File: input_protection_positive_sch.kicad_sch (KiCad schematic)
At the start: 24 parts, among them Q1 SQM120P06, Q2 SQM120P06, U1 ADM1270

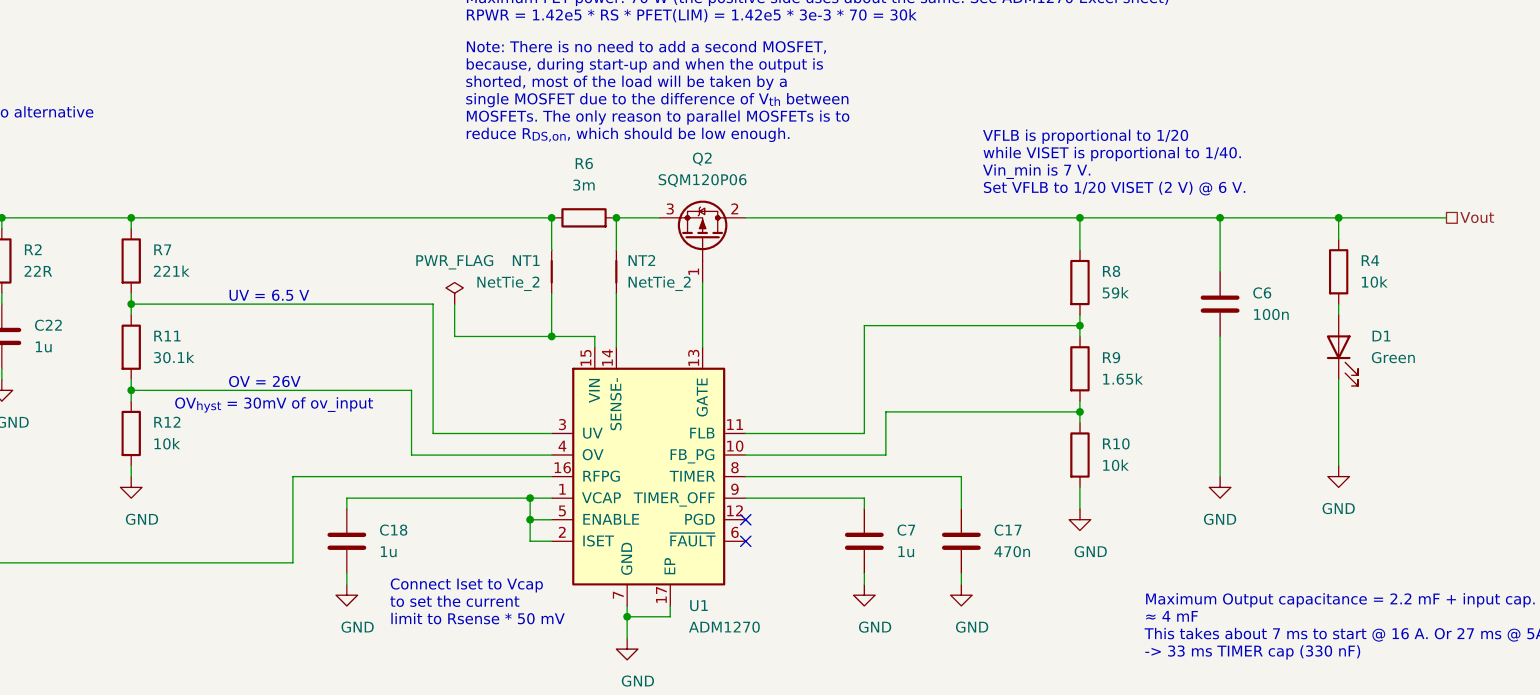
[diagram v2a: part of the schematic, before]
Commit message: Replaced negative side NMOS with SQJQ160E Reduced number of thermal spokes required to 1
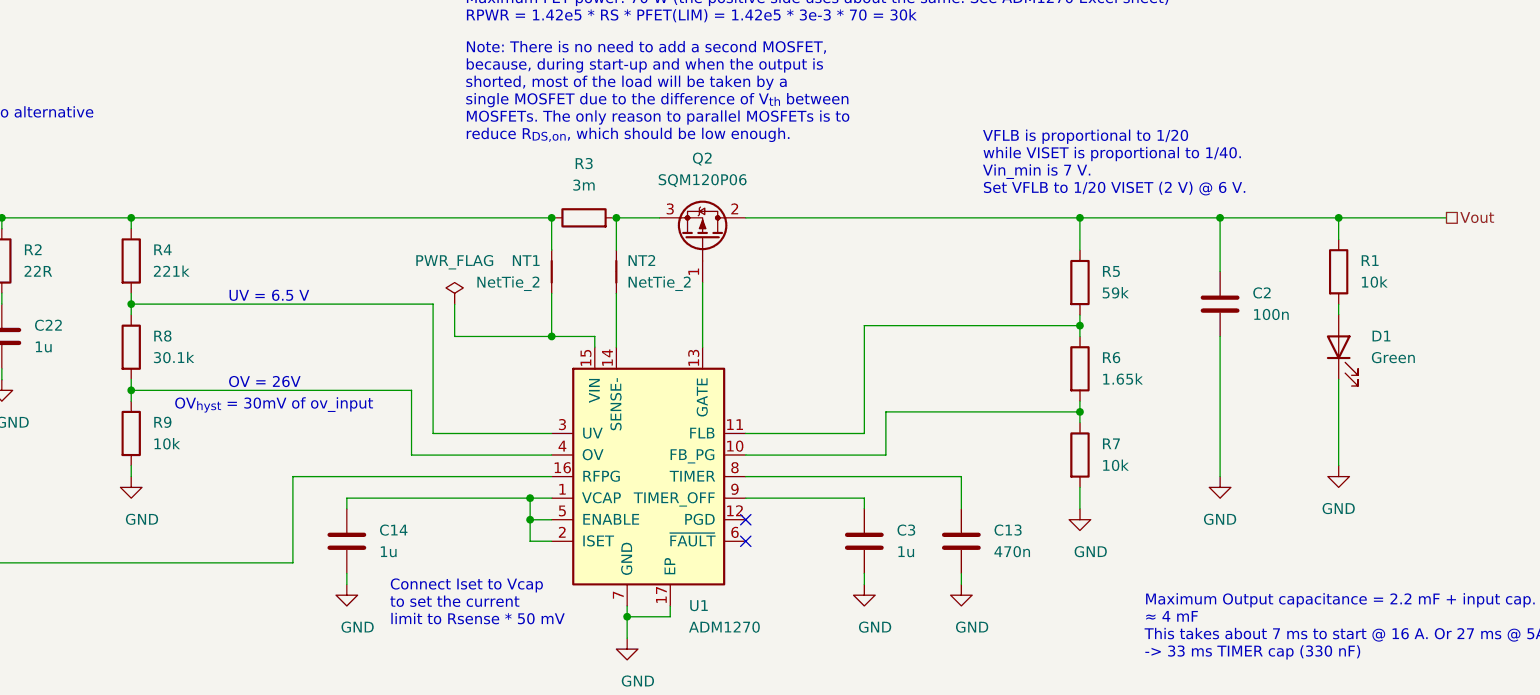
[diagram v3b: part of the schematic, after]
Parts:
- renumbered C17 to C13, C18 to C14, C6 to C2, C7 to C3, R4 to R1, R6 to R3, R7 to R4, R8 to R5, R9 to R6, R10 to R7, R11 to R8, R12 to R9
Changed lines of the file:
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@@
   (symbol (lib_id "Device:R") (at 93.98 80.01 0) (unit 1)
     (in_bom yes) (on_board yes) (dnp no) (fields_autoplaced)
-    (property "Reference" "R11" (at 96.52 78.74 0)
+    (property "Reference" "R8" (at 96.52 78.74 0)
       (effects (font (size 1.27 1.27)) (justify left))
     )
@@
       (project "main"
         (path "/b4ace06a-3ad4-479e-aaa4-d547ecf6903f/f9160387-088e-4a7b-8d58-b2647e07444c"
-          (reference "R11") (unit 1)
+          (reference "R8") (unit 1)
         )
       )
@@
         )
         (path "/b4ace06a-3ad4-479e-aaa4-d547ecf6903f/f9160387-088e-4a7b-8d58-b2647e07444c"
-          (reference "C1") (unit 1)
+          (reference "C15") (unit 1)
         )
         (path "/b4ace06a-3ad4-479e-aaa4-d547ecf6903f/1acfc0a8-4adc-455e-9f2b-420811df0901"
@@
   (symbol (lib_id "Device:R") (at 236.22 71.12 0) (unit 1)
     (in_bom yes) (on_board yes) (dnp no)
-    (property "Reference" "R4" (at 238.76 69.85 0)
+    (property "Reference" "R1" (at 238.76 69.85 0)
       (effects (font (size 1.27 1.27)) (justify left))
     )
@@
       (project "main"
         (path "/b4ace06a-3ad4-479e-aaa4-d547ecf6903f/f9160387-088e-4a7b-8d58-b2647e07444c"
-          (reference "R4") (unit 1)
+          (reference "R1") (unit 1)
         )
         (path "/b4ace06a-3ad4-479e-aaa4-d547ecf6903f/1acfc0a8-4adc-455e-9f2b-420811df0901"
@@
         )
         (path "/b4ace06a-3ad4-479e-aaa4-d547ecf6903f/f9160387-088e-4a7b-8d58-b2647e07444c"
-          (reference "FB2") (unit 1)
+          (reference "FB1") (unit 1)
         )
       )
@@
   (symbol (lib_id "Device:C") (at 222.25 74.93 0) (unit 1)
     (in_bom yes) (on_board yes) (dnp no) (fields_autoplaced)
-    (property "Reference" "C6" (at 226.06 73.66 0)
+    (property "Reference" "C2" (at 226.06 73.66 0)
       (effects (font (size 1.27 1.27)) (justify left))
     )
@@
       (project "main"
         (path "/b4ace06a-3ad4-479e-aaa4-d547ecf6903f/f9160387-088e-4a7b-8d58-b2647e07444c"
-          (reference "C6") (unit 1)
+          (reference "C2") (unit 1)
         )
       )
@@
   (symbol (lib_id "Device:R") (at 205.74 72.39 0) (unit 1)
     (in_bom yes) (on_board yes) (dnp no) (fields_autoplaced)
-    (property "Reference" "R8" (at 208.28 71.12 0)
+    (property "Reference" "R5" (at 208.28 71.12 0)
       (effects (font (size 1.27 1.27)) (justify left))
     )
@@
       (project "main"
         (path "/b4ace06a-3ad4-479e-aaa4-d547ecf6903f/f9160387-088e-4a7b-8d58-b2647e07444c"
-          (reference "R8") (unit 1)
+          (reference "R5") (unit 1)
         )
       )
@@
         )
         (path "/b4ace06a-3ad4-479e-aaa4-d547ecf6903f/f9160387-088e-4a7b-8d58-b2647e07444c"
-          (reference "R1") (unit 1)
+          (reference "R10") (unit 1)
         )
         (path "/b4ace06a-3ad4-479e-aaa4-d547ecf6903f/1acfc0a8-4adc-455e-9f2b-420811df0901"
@@
   (symbol (lib_id "Device:R") (at 205.74 82.55 0) (unit 1)
     (in_bom yes) (on_board yes) (dnp no) (fields_autoplaced)
-    (property "Reference" "R9" (at 208.28 81.28 0)
+    (property "Reference" "R6" (at 208.28 81.28 0)
       (effects (font (size 1.27 1.27)) (justify left))
     )
@@
       (project "main"
         (path "/b4ace06a-3ad4-479e-aaa4-d547ecf6903f/f9160387-088e-4a7b-8d58-b2647e07444c"
-          (reference "R9") (unit 1)
+          (reference "R6") (unit 1)
         )
       )
@@
         )
         (path "/b4ace06a-3ad4-479e-aaa4-d547ecf6903f/f9160387-088e-4a7b-8d58-b2647e07444c"
-          (reference "R5") (unit 1)
+          (reference "R2") (unit 1)
         )
         (path "/b4ace06a-3ad4-479e-aaa4-d547ecf6903f/1acfc0a8-4adc-455e-9f2b-420811df0901"
@@
   (symbol (lib_id "Device:C") (at 180.34 102.87 0) (unit 1)
     (in_bom yes) (on_board yes) (dnp no) (fields_autoplaced)
-    (property "Reference" "C7" (at 184.15 101.6 0)
+    (property "Reference" "C3" (at 184.15 101.6 0)
       (effects (font (size 1.27 1.27)) (justify left))
     )
@@
       (project "main"
         (path "/b4ace06a-3ad4-479e-aaa4-d547ecf6903f/f9160387-088e-4a7b-8d58-b2647e07444c"
-          (reference "C7") (unit 1)
+          (reference "C3") (unit 1)
         )
       )
@@
   (symbol (lib_id "Device:C") (at 119.38 102.87 0) (unit 1)
     (in_bom yes) (on_board yes) (dnp no) (fields_autoplaced)
-    (property "Reference" "C18" (at 123.19 101.6 0)
+    (property "Reference" "C14" (at 123.19 101.6 0)
       (effects (font (size 1.27 1.27)) (justify left))
     )
@@
       (project "main"
         (path "/b4ace06a-3ad4-479e-aaa4-d547ecf6903f/f9160387-088e-4a7b-8d58-b2647e07444c"
-          (reference "C18") (unit 1)
+          (reference "C14") (unit 1)
         )
       )
@@
   (symbol (lib_id "Device:R") (at 93.98 69.85 0) (unit 1)
     (in_bom yes) (on_board yes) (dnp no) (fields_autoplaced)
-    (property "Reference" "R7" (at 96.52 68.58 0)
+    (property "Reference" "R4" (at 96.52 68.58 0)
       (effects (font (size 1.27 1.27)) (justify left))
     )
@@
       (project "main"
         (path "/b4ace06a-3ad4-479e-aaa4-d547ecf6903f/f9160387-088e-4a7b-8d58-b2647e07444c"
-          (reference "R7") (unit 1)
+          (reference "R4") (unit 1)
         )
       )
@@
   (symbol (lib_id "Device:R") (at 147.32 64.77 90) (unit 1)
     (in_bom yes) (on_board yes) (dnp no) (fields_autoplaced)
-    (property "Reference" "R6" (at 147.32 58.42 90)
+    (property "Reference" "R3" (at 147.32 58.42 90)
       (effects (font (size 1.27 1.27)))
     )
@@
       (project "main"
         (path "/b4ace06a-3ad4-479e-aaa4-d547ecf6903f/f9160387-088e-4a7b-8d58-b2647e07444c"
-          (reference "R6") (unit 1)
+          (reference "R3") (unit 1)
         )
       )
@@
   (symbol (lib_id "Device:R") (at 93.98 90.17 0) (unit 1)
     (in_bom yes) (on_board yes) (dnp no) (fields_autoplaced)
-    (property "Reference" "R12" (at 96.52 88.9 0)
+    (property "Reference" "R9" (at 96.52 88.9 0)
       (effects (font (size 1.27 1.27)) (justify left))
     )
@@
       (project "main"
         (path "/b4ace06a-3ad4-479e-aaa4-d547ecf6903f/f9160387-088e-4a7b-8d58-b2647e07444c"
-          (reference "R12") (unit 1)
+          (reference "R9") (unit 1)
         )
       )
@@
   (symbol (lib_id "Device:C") (at 191.77 102.87 0) (unit 1)
     (in_bom yes) (on_board yes) (dnp no) (fields_autoplaced)
-    (property "Reference" "C17" (at 195.58 101.6 0)
+    (property "Reference" "C13" (at 195.58 101.6 0)
       (effects (font (size 1.27 1.27)) (justify left))
     )
@@
       (project "main"
         (path "/b4ace06a-3ad4-479e-aaa4-d547ecf6903f/f9160387-088e-4a7b-8d58-b2647e07444c"
-          (reference "C17") (unit 1)
+          (reference "C13") (unit 1)
         )
       )
@@
   (symbol (lib_id "Device:R") (at 205.74 92.71 0) (unit 1)
     (in_bom yes) (on_board yes) (dnp no) (fields_autoplaced)
-    (property "Reference" "R10" (at 208.28 91.44 0)
+    (property "Reference" "R7" (at 208.28 91.44 0)
       (effects (font (size 1.27 1.27)) (justify left))
     )
@@
       (project "main"
         (path "/b4ace06a-3ad4-479e-aaa4-d547ecf6903f/f9160387-088e-4a7b-8d58-b2647e07444c"
-          (reference "R10") (unit 1)
+          (reference "R7") (unit 1)
         )
       )
@@
         )
         (path "/b4ace06a-3ad4-479e-aaa4-d547ecf6903f/f9160387-088e-4a7b-8d58-b2647e07444c"
-          (reference "C5") (unit 1)
-        )
-        (path "/b4ace06a-3ad4-479e-aaa4-d547ecf6903f/1acfc0a8-4adc-455e-9f2b-420811df0901"
+          (reference "C1") (unit 1)
+        )
+        (path "/b4ace06a-3ad4-479e-aaa4-d547ecf6903f/1acfc0a8-4adc-455e-9f2b-420811df0901"

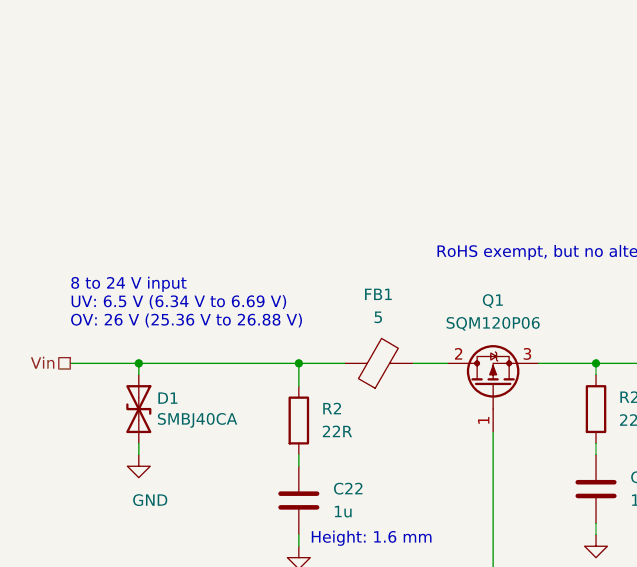
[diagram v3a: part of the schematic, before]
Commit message: Reduced datasheet absolute maximum voltage to ±48 V, because the TVS diodes start conducting considerably at 48 V
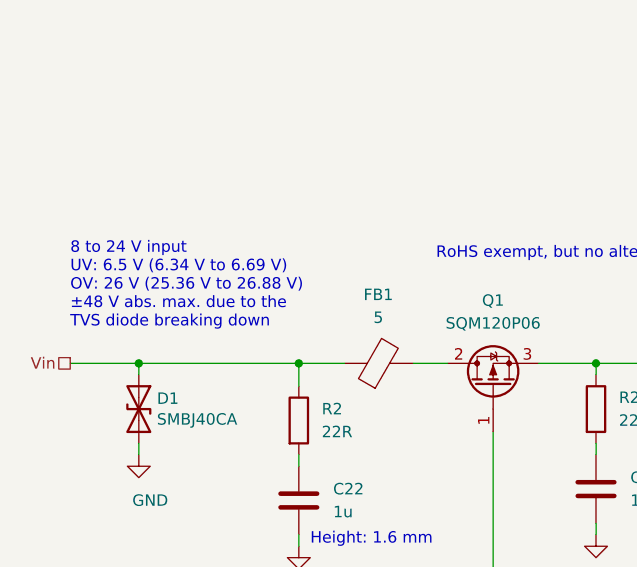
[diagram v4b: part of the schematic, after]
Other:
- note added: "8 to 24 V input UV: 6.5 V (6.34 V to 6.69 V) OV: 26 V (25.36 V to 26.88 V) ±48 V abs. max. due to the TVS diode breaking down"
- note removed: "8 to 24 V input UV: 6.5 V (6.34 V to 6.69 V) OV: 26 V (25.36 V to 26.88 V)"
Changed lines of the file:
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@@
     (effects (font (size 1.27 1.27)) (justify left bottom))
   )
-  (text "8 to 24 V input\nUV: 6.5 V (6.34 V to 6.69 V)\nOV: 26 V (25.36 V to 26.88 V)"
+  (text "8 to 24 V input\nUV: 6.5 V (6.34 V to 6.69 V)\nOV: 26 V (25.36 V to 26.88 V)\n±48 V abs. max. due to the\nTVS diode breaking down"
     (at 20.32 60.96 0)
     (effects (font (size 1.27 1.27)) (justify left bottom))

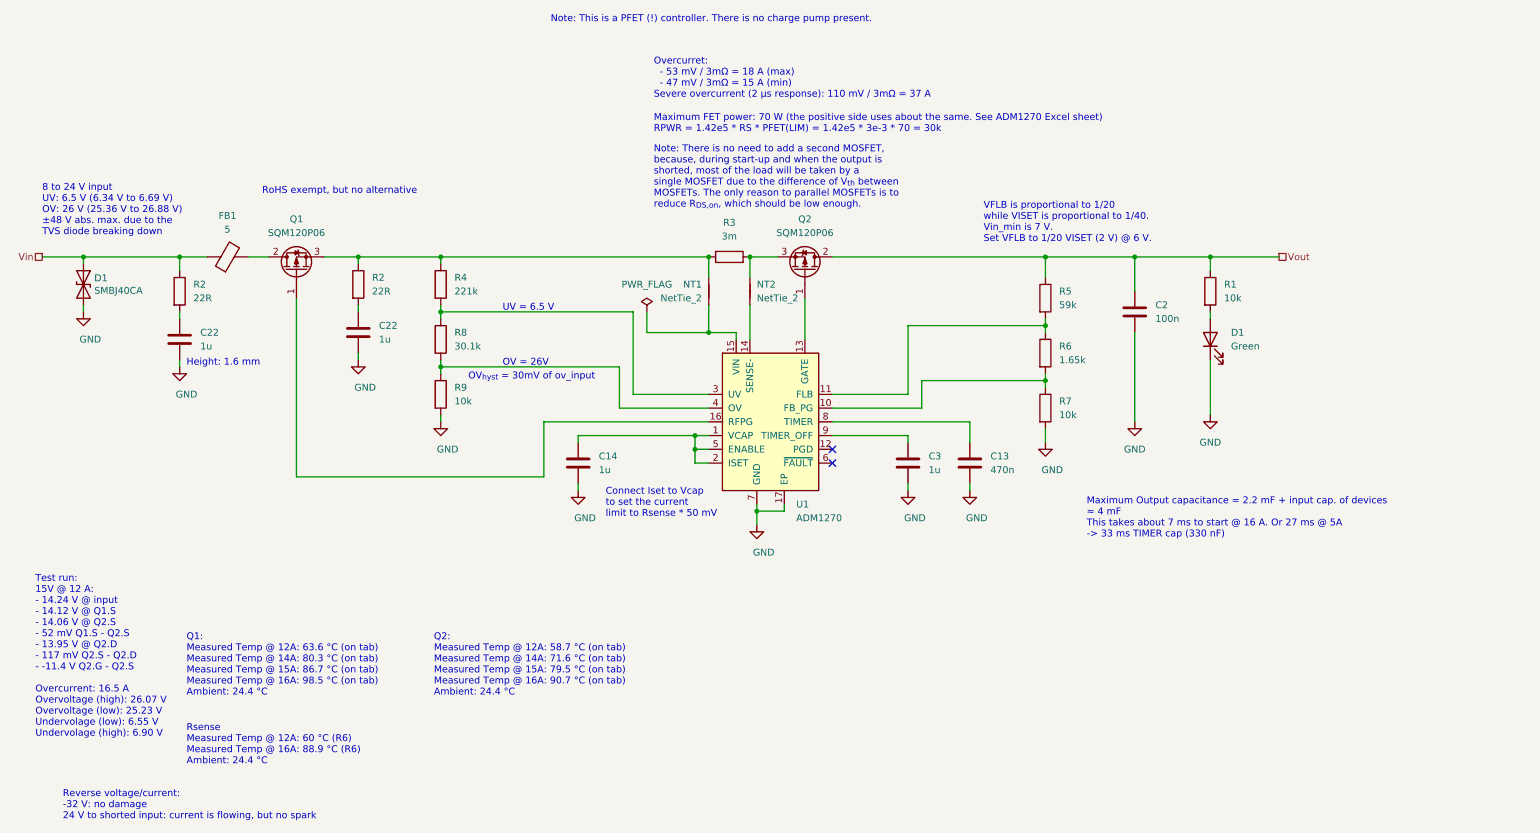
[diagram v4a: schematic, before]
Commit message: Added thermal jumpers Increased copper area at the PMOS and the current sense resistors
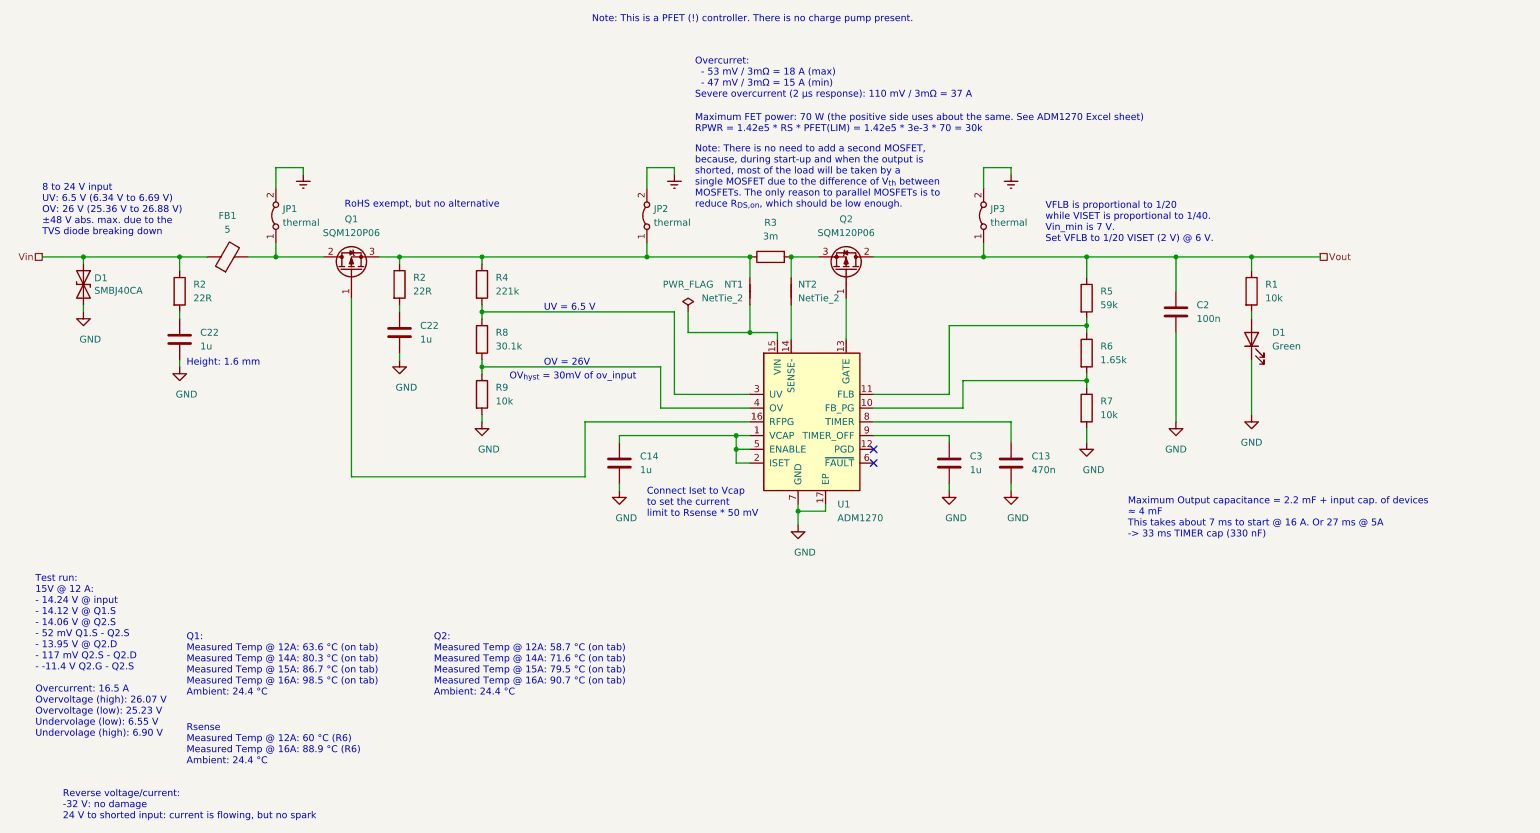
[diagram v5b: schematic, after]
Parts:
- added JP1, JP2, JP3: thermal, Resistor_SMD:R_0612_1632Metric, symbol Jumper:Jumper_2_Bridged
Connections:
- net Vout: now also JP3.1 (A)
- net at FB1.2, Q1.2 (D): now also JP1.1 (A)
- net at NT1.2, Q1.3 (S), R2.1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: now also JP2.1 (A)
- new net Earth: JP1.2 (B), JP2.2 (B), JP3.2 (B)
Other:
- moved on the sheet: C13, C14, C2, C22, C3, D1, NT1, NT2, Q1, Q2, R1, R2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

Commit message: Updated RoHS information
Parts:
- JP1, JP2, JP3: PN THJP0612ABT1 -> THJP0612AST1; RoHS (none) -> Yes; Temperature (none) -> Tstorage = –65 °C to 150 °C
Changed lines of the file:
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@@
       (effects (font (size 1.27 1.27)) hide)
     )
-    (property "PN" "THJP0612ABT1" (at 194.31 57.15 0)
+    (property "PN" "THJP0612AST1" (at 194.31 57.15 0)
+      (effects (font (size 1.27 1.27)) hide)
+    )
+    (property "RoHS" "Yes" (at 194.31 57.15 0)
+      (effects (font (size 1.27 1.27)) hide)
+    )
+    (property "Temperature" "Tstorage = –65 °C to 150 °C" (at 194.31 57.15 0)
       (effects (font (size 1.27 1.27)) hide)
     )
@@
       (effects (font (size 1.27 1.27)) hide)
     )
-    (property "PN" "THJP0612ABT1" (at 63.5 57.15 0)
+    (property "PN" "THJP0612AST1" (at 63.5 57.15 0)
+      (effects (font (size 1.27 1.27)) hide)
+    )
+    (property "RoHS" "Yes" (at 63.5 57.15 0)
+      (effects (font (size 1.27 1.27)) hide)
+    )
+    (property "Temperature" "Tstorage = –65 °C to 150 °C" (at 63.5 57.15 0)
       (effects (font (size 1.27 1.27)) hide)
     )
@@
       (effects (font (size 1.27 1.27)) hide)
     )
-    (property "PN" "THJP0612ABT1" (at 132.08 57.15 0)
-      (effects (font (size 1.27 1.27)) hide)
-    )
+    (property "PN" "THJP0612AST1" (at 132.08 57.15 0)
+      (effects (font (size 1.27 1.27)) hide)
+    )
+    (property "RoHS" "Yes" (at 132.08 57.15 0)
+      (effects (font (size 1.27 1.27)) hide)
+    )
+    (property "Temperature" "Tstorage = –65 °C to 150 °C" (at 132.08 57.15 0)
+      (effects (font (size 1.27 1.27)) hide)
+    )
